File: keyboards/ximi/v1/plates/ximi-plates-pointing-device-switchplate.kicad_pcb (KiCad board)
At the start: 2 copper layers, 168.7 x 95.6 mm, 31 parts, among them J2 USB_C_Receptacle_USB2.0, J7 AudioJack4dpb, SW1 SW_Push, SW10 SW_Push, SW11 SW_Push, SW12 SW_Push, SW13 SW_Push, SW14 SW_Push, SW15 SW_Push, SW16 SW_Push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

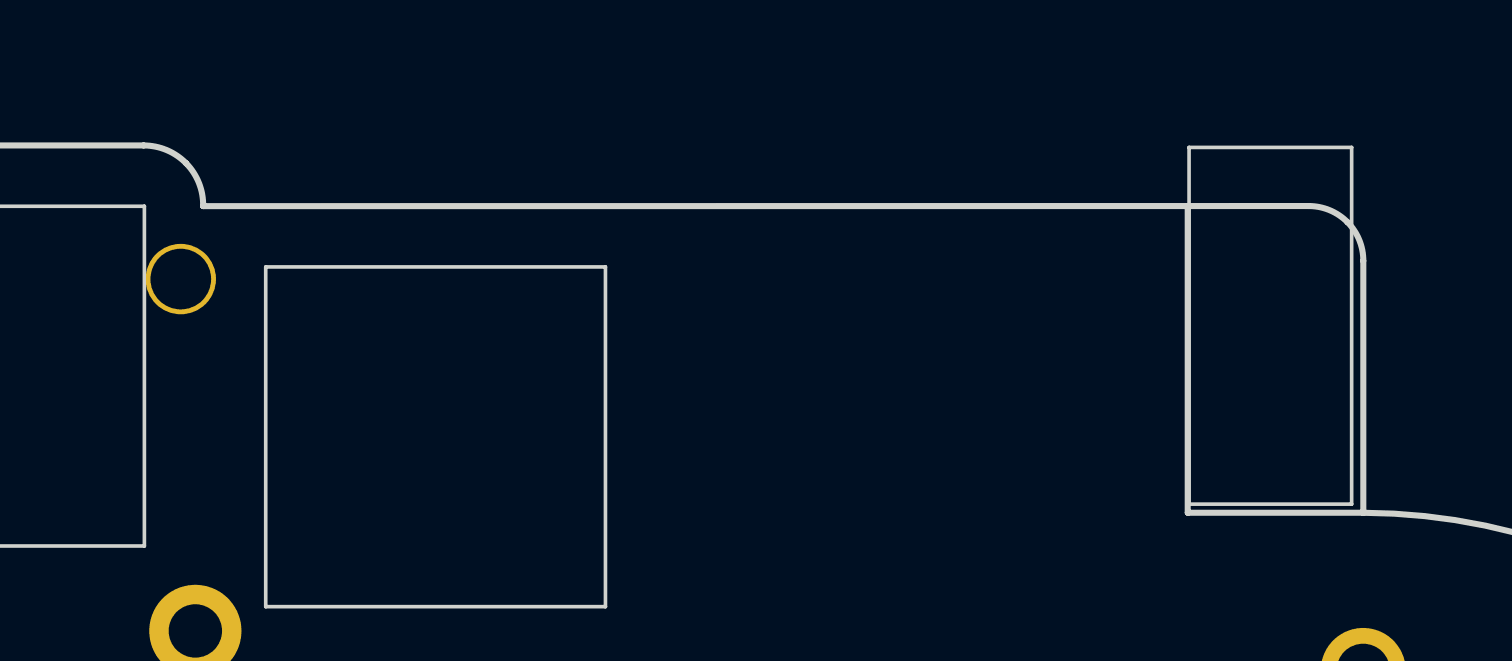
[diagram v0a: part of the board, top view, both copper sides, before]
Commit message: finished up basic pointing device plates, along with the templates
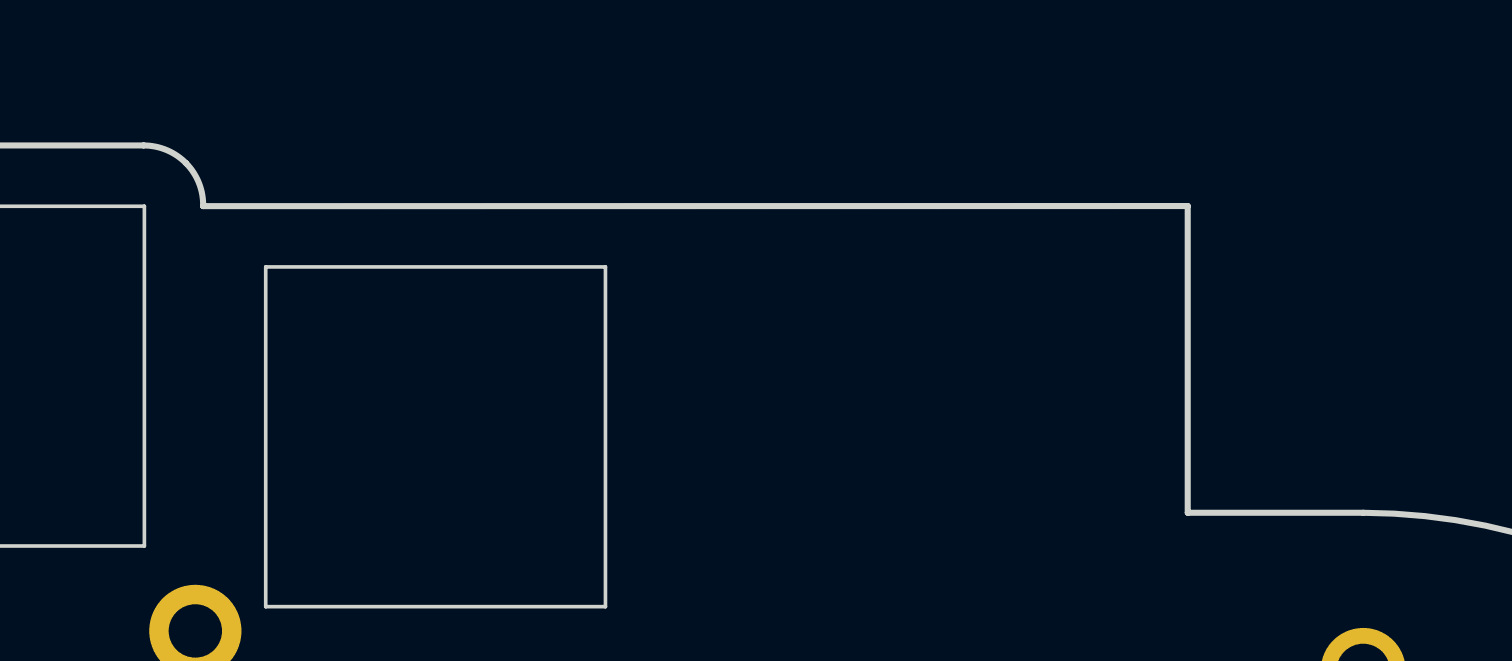
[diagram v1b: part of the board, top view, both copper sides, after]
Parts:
- removed J2: USB_C_Receptacle_USB2.0, fingerpunch-plates:USB_C_Receptacle_HRO_TYPE-C-31-M-12
- removed J7: AudioJack4dpb, fingerpunch-plates:TRRS-PJ-320A
- removed SW50: SW_Push, fingerpunch-plates:MountingHole_2.5mm
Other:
- outline, holes or cut-outs redrawn
